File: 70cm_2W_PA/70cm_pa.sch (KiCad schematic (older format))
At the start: 51 parts, among them J3 Conn_01x02, U1 M68710L, U2 MIC5205YM5, U3 SN74LV1T08, U4 LM75B

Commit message: M68710L: more layout
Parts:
- added C7: 2u2, Capacitor_SMD:C_0805_2012Metric, symbol Device:C
- C6: value 10u -> 100u; footprint Capacitor_SMD:C_1206_3216Metric -> Capacitor_Tantalum_SMD:CP_EIA-6032-15_Kemet-U; symbol Device:C -> Device:CP
- renumbered C9 to C10, C10 to C11, C11 to C12, C7 to C8, C8 to C9
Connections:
- net GND: now also C7.2
- net V_supply: now also C7.1
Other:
- moved on the sheet: R7
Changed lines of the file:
@@
 $EndComp
 $Comp
-L power:GND #PWR026
+L power:GND #PWR027
 U 1 1 5DB17A29
 P 5550 7450
-F 0 "#PWR026" H 5550 7200 50  0001 C CNN
+F 0 "#PWR027" H 5550 7200 50  0001 C CNN
 F 1 "GND" H 5555 7277 50  0000 C CNN
 F 2 "" H 5550 7450 50  0001 C CNN
@@
 $EndComp
 $Comp
-L power:GND #PWR027
+L power:GND #PWR028
 U 1 1 5DB18393
 P 5900 7450
-F 0 "#PWR027" H 5900 7200 50  0001 C CNN
+F 0 "#PWR028" H 5900 7200 50  0001 C CNN
 F 1 "GND" H 5905 7277 50  0000 C CNN
 F 2 "" H 5900 7450 50  0001 C CNN
@@
 $EndComp
 $Comp
-L power:GND #PWR028
+L power:GND #PWR029
 U 1 1 5DB1850A
 P 6250 7450
-F 0 "#PWR028" H 6250 7200 50  0001 C CNN
+F 0 "#PWR029" H 6250 7200 50  0001 C CNN
 F 1 "GND" H 6255 7277 50  0000 C CNN
 F 2 "" H 6250 7450 50  0001 C CNN
@@
 $EndComp
 $Comp
-L power:GND #PWR029
+L power:GND #PWR030
 U 1 1 5DB18617
 P 6600 7450
-F 0 "#PWR029" H 6600 7200 50  0001 C CNN
+F 0 "#PWR030" H 6600 7200 50  0001 C CNN
 F 1 "GND" H 6605 7277 50  0000 C CNN
 F 2 "" H 6600 7450 50  0001 C CNN
@@
 	2750 1700 3400 1700
 $Comp
-L Device:C C6
+L Device:CP C6
 U 1 1 5DB24127
-P 2300 3750
-F 0 "C6" H 2415 3796 50  0000 L CNN
-F 1 "10u" H 2415 3705 50  0000 L CNN
-F 2 "Capacitor_SMD:C_1206_3216Metric" H 2338 3600 50  0001 C CNN
-F 3 "~" H 2300 3750 50  0001 C CNN
-	1    2300 3750
+P 2150 3750
+F 0 "C6" H 2265 3796 50  0000 L CNN
+F 1 "100u" H 2265 3705 50  0000 L CNN
+F 2 "Capacitor_Tantalum_SMD:CP_EIA-6032-15_Kemet-U" H 2188 3600 50  0001 C CNN
+F 3 "~" H 2150 3750 50  0001 C CNN
+	1    2150 3750
 	1    0    0    -1
 $EndComp
@@
 L power:GND #PWR014
 U 1 1 5DB2442A
-P 2300 3900
-F 0 "#PWR014" H 2300 3650 50  0001 C CNN
-F 1 "GND" H 2305 3727 50  0000 C CNN
-F 2 "" H 2300 3900 50  0001 C CNN
-F 3 "" H 2300 3900 50  0001 C CNN
-	1    2300 3900
+P 2150 3900
+F 0 "#PWR014" H 2150 3650 50  0001 C CNN
+F 1 "GND" H 2155 3727 50  0000 C CNN
+F 2 "" H 2150 3900 50  0001 C CNN
+F 3 "" H 2150 3900 50  0001 C CNN
+	1    2150 3900
 	1    0    0    -1
 $EndComp
@@
 $EndComp
 $Comp
-L power:GND #PWR025
+L power:GND #PWR026
 U 1 1 5DB3243A
 P 5150 6650
-F 0 "#PWR025" H 5150 6400 50  0001 C CNN
+F 0 "#PWR026" H 5150 6400 50  0001 C CNN
 F 1 "GND" H 5155 6477 50  0000 C CNN
 F 2 "" H 5150 6650 50  0001 C CNN
@@
 There are several pin compatible regulators,\nso different options could be evaluated.
 $Comp
-L power:GND #PWR016
+L power:GND #PWR017
 U 1 1 5DB02BC8
 P 5400 4150
-F 0 "#PWR016" H 5400 3900 50  0001 C CNN
+F 0 "#PWR017" H 5400 3900 50  0001 C CNN
 F 1 "GND" H 5405 3977 50  0000 C CNN
 F 2 "" H 5400 4150 50  0001 C CNN
@@
 $EndComp
 $Comp
-L Device:C C8
+L Device:C C9
 U 1 1 5DB11E39
 P 7550 3900
-F 0 "C8" H 7665 3946 50  0000 L CNN
+F 0 "C9" H 7665 3946 50  0000 L CNN
 F 1 "2u2" H 7665 3855 50  0000 L CNN
 F 2 "Capacitor_SMD:C_0805_2012Metric" H 7588 3750 50  0001 C CNN
@@
 $EndComp
 $Comp
-L power:GND #PWR017
+L power:GND #PWR018
 U 1 1 5DB1212E
 P 7550 4350
-F 0 "#PWR017" H 7550 4100 50  0001 C CNN
+F 0 "#PWR018" H 7550 4100 50  0001 C CNN
 F 1 "GND" H 7555 4177 50  0000 C CNN
 F 2 "" H 7550 4350 50  0001 C CNN
@@
 $EndComp
 $Comp
-L Device:C C7
+L Device:C C8
 U 1 1 5DB19997
 P 4550 3900
-F 0 "C7" H 4665 3946 50  0000 L CNN
+F 0 "C8" H 4665 3946 50  0000 L CNN
 F 1 "2u2" H 4665 3855 50  0000 L CNN
 F 2 "Capacitor_SMD:C_0805_2012Metric" H 4588 3750 50  0001 C CNN
@@
 $EndComp
 $Comp
-L power:GND #PWR015
+L power:GND #PWR016
 U 1 1 5DB19DB0
 P 4550 4050
-F 0 "#PWR015" H 4550 3800 50  0001 C CNN
+F 0 "#PWR016" H 4550 3800 50  0001 C CNN
 F 1 "GND" H 4555 3877 50  0000 C CNN
 F 2 "" H 4550 4050 50  0001 C CNN
@@
 Vbias
 $Comp
-L power:GND #PWR022
+L power:GND #PWR023
 U 1 1 5DB70B3E
 P 2700 5750
-F 0 "#PWR022" H 2700 5500 50  0001 C CNN
+F 0 "#PWR023" H 2700 5500 50  0001 C CNN
 F 1 "GND" H 2705 5577 50  0000 C CNN
 F 2 "" H 2700 5750 50  0001 C CNN
@@
 	2300 5600 2400 5600
 $Comp
-L power:GND #PWR024
+L power:GND #PWR025
 U 1 1 5DB7EA8B
 P 1550 5900
-F 0 "#PWR024" H 1550 5650 50  0001 C CNN
+F 0 "#PWR025" H 1550 5650 50  0001 C CNN
 F 1 "GND" H 1555 5727 50  0000 C CNN
 F 2 "" H 1550 5900 50  0001 C CNN
@@
 Wire Wire Line
 	3800 950  3800 1400
-Wire Wire Line
-	1750 3600 2300 3600
 $Comp
 L Device:R R7
 U 1 1 5DC0951D
-P 2750 3600
-F 0 "R7" V 2543 3600 50  0000 C CNN
-F 1 "0" V 2634 3600 50  0000 C CNN
-F 2 "Resistor_SMD:R_0805_2012Metric" V 2680 3600 50  0001 C CNN
-F 3 "~" H 2750 3600 50  0001 C CNN
-	1    2750 3600
+P 2950 3600
+F 0 "R7" V 2743 3600 50  0000 C CNN
+F 1 "0" V 2834 3600 50  0000 C CNN
+F 2 "Resistor_SMD:R_0805_2012Metric" V 2880 3600 50  0001 C CNN
+F 3 "~" H 2950 3600 50  0001 C CNN
+	1    2950 3600
 	0    1    1    0
 $EndComp
-Wire Wire Line
-	2600 3600 2300 3600
-Connection ~ 2300 3600
 Text Label 1750 3600 0    50   ~ 0
 V_supply
 Wire Wire Line
-	2900 3600 3100 3600
-Text Label 3200 3600 0    50   ~ 0
+	3100 3600 3300 3600
+Text Label 3400 3600 0    50   ~ 0
 PA_VDD
 $Comp
-L power:GND #PWR023
+L power:GND #PWR024
 U 1 1 5DC14CBC
 P 900 5800
-F 0 "#PWR023" H 900 5550 50  0001 C CNN
+F 0 "#PWR024" H 900 5550 50  0001 C CNN
 F 1 "GND" H 905 5627 50  0000 C CNN
 F 2 "" H 900 5800 50  0001 C CNN
@@
 L power:PWR_FLAG #FLG01
 U 1 1 5DC5B5D3
-P 3100 3600
-F 0 "#FLG01" H 3100 3675 50  0001 C CNN
-F 1 "PWR_FLAG" H 3100 3773 50  0000 C CNN
-F 2 "" H 3100 3600 50  0001 C CNN
-F 3 "~" H 3100 3600 50  0001 C CNN
-	1    3100 3600
-	1    0    0    -1
-$EndComp
-Wire Wire Line
-	3200 3600 3100 3600
-Connection ~ 3100 3600
+P 3300 3600
+F 0 "#FLG01" H 3300 3675 50  0001 C CNN
+F 1 "PWR_FLAG" H 3300 3773 50  0000 C CNN
+F 2 "" H 3300 3600 50  0001 C CNN
+F 3 "~" H 3300 3600 50  0001 C CNN
+	1    3300 3600
+	1    0    0    -1
+$EndComp
+Wire Wire Line
+	3400 3600 3300 3600
+Connection ~ 3300 3600
 $Comp
 L 74xGxx:74LVC1G08 U3
@@
 $EndComp
 $Comp
-L Device:C C9
+L Device:C C10
 U 1 1 5DAFCA3B
 P 5700 4500
-F 0 "C9" H 5815 4546 50  0000 L CNN
+F 0 "C10" H 5815 4546 50  0000 L CNN
 F 1 "1n" H 5815 4455 50  0000 L CNN
 F 2 "Capacitor_SMD:C_0805_2012Metric" H 5738 4350 50  0001 C CNN
@@
 $EndComp
 $Comp
-L power:GND #PWR019
+L power:GND #PWR020
 U 1 1 5DC2C60C
 P 7150 4650
-F 0 "#PWR019" H 7150 4400 50  0001 C CNN
+F 0 "#PWR020" H 7150 4400 50  0001 C CNN
 F 1 "GND" H 7155 4477 50  0000 C CNN
 F 2 "" H 7150 4650 50  0001 C CNN
@@
 $EndComp
 $Comp
-L power:GND #PWR018
+L power:GND #PWR019
 U 1 1 5DAFE126
 P 5700 4650
-F 0 "#PWR018" H 5700 4400 50  0001 C CNN
+F 0 "#PWR019" H 5700 4400 50  0001 C CNN
 F 1 "GND" H 5705 4477 50  0000 C CNN
 F 2 "" H 5700 4650 50  0001 C CNN
@@
 Connection ~ 7550 3750
 $Comp
-L Device:C C10
+L Device:C C11
 U 1 1 5DB372D9
 P 1950 5050
-F 0 "C10" H 2065 5096 50  0000 L CNN
+F 0 "C11" H 2065 5096 50  0000 L CNN
 F 1 "100n" H 2065 5005 50  0000 L CNN
 F 2 "Capacitor_SMD:C_0805_2012Metric" H 1988 4900 50  0001 C CNN
@@
 $EndComp
 $Comp
-L power:GND #PWR020
+L power:GND #PWR021
 U 1 1 5DB3BC87
 P 1950 5200
-F 0 "#PWR020" H 1950 4950 50  0001 C CNN
+F 0 "#PWR021" H 1950 4950 50  0001 C CNN
 F 1 "GND" H 1955 5027 50  0000 C CNN
 F 2 "" H 1950 5200 50  0001 C CNN
@@
 Connection ~ 1950 4900
 $Comp
-L Device:C C11
+L Device:C C12
 U 1 1 5DB547EB
 P 4750 5050
-F 0 "C11" H 4865 5096 50  0000 L CNN
+F 0 "C12" H 4865 5096 50  0000 L CNN
 F 1 "100n" H 4865 5005 50  0000 L CNN
 F 2 "Capacitor_SMD:C_0805_2012Metric" H 4788 4900 50  0001 C CNN
@@
 $EndComp
 $Comp
-L power:GND #PWR021
+L power:GND #PWR022
 U 1 1 5DB54F87
 P 4750 5200
-F 0 "#PWR021" H 4750 4950 50  0001 C CNN
+F 0 "#PWR022" H 4750 4950 50  0001 C CNN
 F 1 "GND" H 4755 5027 50  0000 C CNN
 F 2 "" H 4750 5200 50  0001 C CNN
@@
 Wire Wire Line
 	5150 6650 5650 6650
+Wire Wire Line
+	2150 3600 1750 3600
+Connection ~ 2150 3600
+$Comp
+L power:GND #PWR015
+U 1 1 5DB8951F
+P 2550 3900
+F 0 "#PWR015" H 2550 3650 50  0001 C CNN
+F 1 "GND" H 2555 3727 50  0000 C CNN
+F 2 "" H 2550 3900 50  0001 C CNN
+F 3 "" H 2550 3900 50  0001 C CNN
+	1    2550 3900
+	1    0    0    -1
+$EndComp
+Wire Wire Line
+	2150 3600 2550 3600
+$Comp
+L Device:C C7
+U 1 1 5DB8C3D6
+P 2550 3750
+F 0 "C7" H 2665 3796 50  0000 L CNN
+F 1 "2u2" H 2665 3705 50  0000 L CNN
+F 2 "Capacitor_SMD:C_0805_2012Metric" H 2588 3600 50  0001 C CNN
+F 3 "~" H 2550 3750 50  0001 C CNN
+	1    2550 3750
+	1    0    0    -1
+$EndComp
+Connection ~ 2550 3600
+Wire Wire Line
+	2550 3600 2800 3600
 $EndSCHEMATC

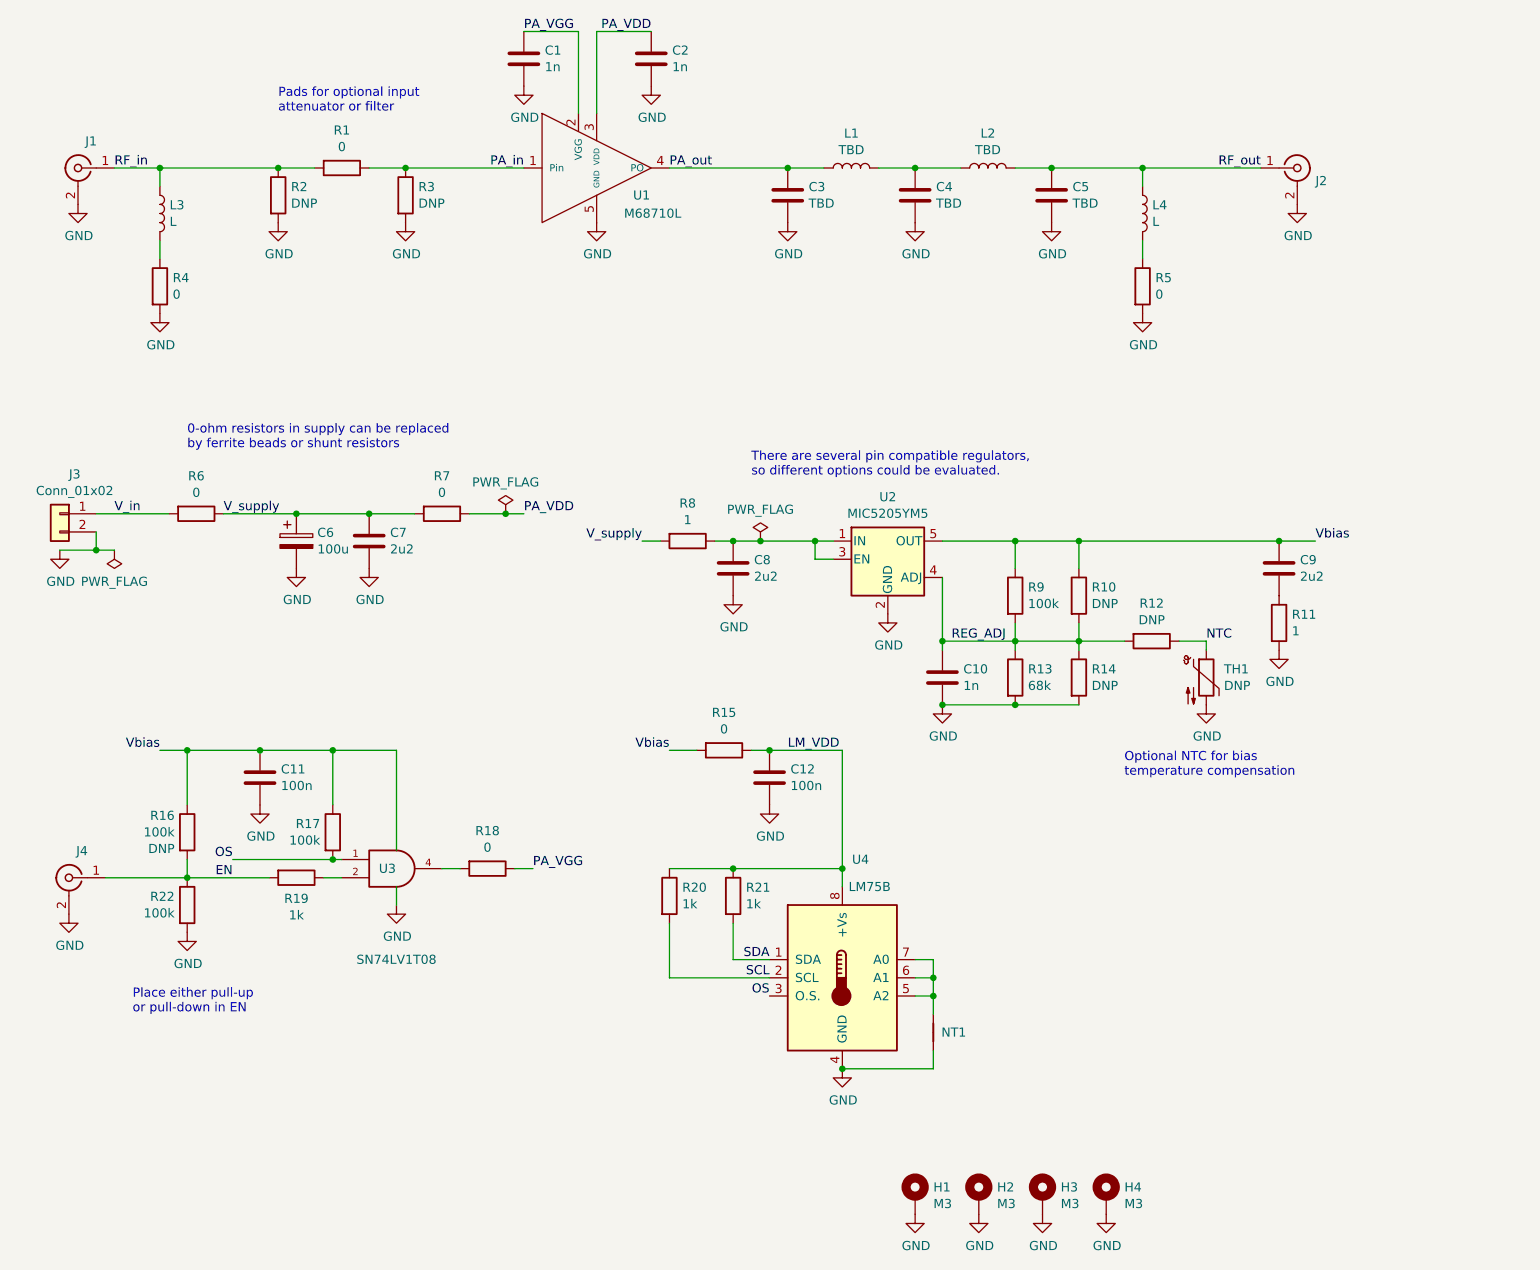
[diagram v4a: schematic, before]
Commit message: M68710L: remove LM75
LM75 operated from the gate bias supply which could become a problem
if bias below 2.8 V is desired. Different supplies might also become
a problem if the I2C were connected to external logic.

LM75 also took more PCB area.
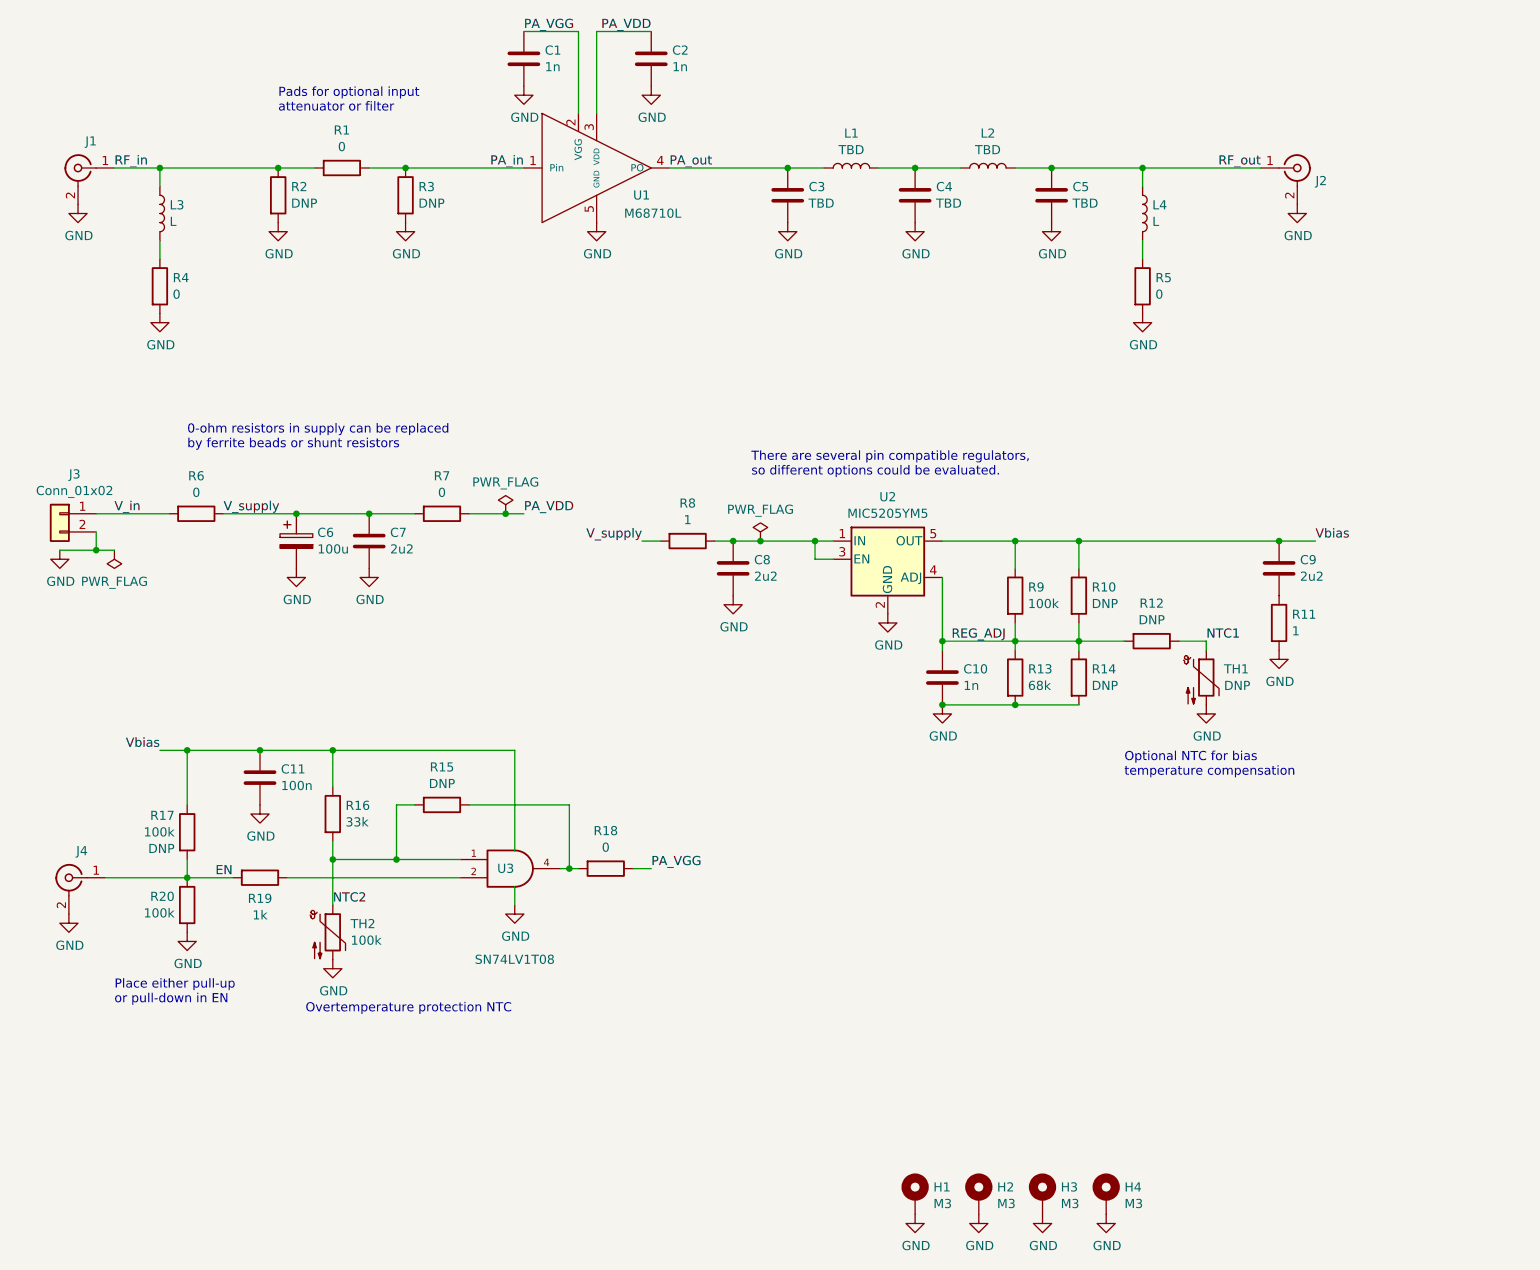
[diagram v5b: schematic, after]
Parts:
- removed C12: 100n, Capacitor_SMD:C_0805_2012Metric, symbol Device:C
- removed NT1: ~, NetTie:NetTie-2_SMD_Pad0.5mm, symbol Device:Net-Tie_2
- removed R20, R21: 1k, Resistor_SMD:R_0805_2012Metric, symbol Device:R
- removed U4: LM75B, Package_SO:SOIC-8_3.9x4.9mm_P1.27mm, symbol Sensor_Temperature:LM75B
- added TH2: 100k, Resistor_SMD:R_0805_2012Metric, symbol Device:Thermistor_NTC
- R15: value 0 -> ~; DNP (none) -> DNP
- R16: renamed from R17; value 100k -> 33k
- renumbered R16 to R17, R22 to R20
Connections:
- net LM_VDD is gone; now on an unnamed net: R15.1
- net GND: now also TH2.2
- net VCC: no longer R15.2
- net NTC renamed NTC1
- net OS renamed NTC2
- net NTC2: now also R15.2, TH2.1
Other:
- note added: "Overtemperature protection NTC"
- moved on the sheet: R16, R18, R19, U3

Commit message: M68710L: everything is connected again
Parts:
- removed C11: 100n, Capacitor_SMD:C_0805_2012Metric, symbol Device:C
- R15: value ~ -> 100k
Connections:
- net GND: now also C9.2; no longer R11.2
- net VCC: now also R11.2; no longer R10.1, R9.1, U2.5 (OUT)
- net REG_OUT: now reaches R11.1
- net REG_OUT: now also R10.1, R9.1, U2.5 (OUT); no longer C9.2
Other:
- moved on the sheet: C9, J4, R11, R15, R16, R17, R18, R19, R20, TH2, U3
